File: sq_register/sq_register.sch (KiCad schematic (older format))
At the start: 1 part, among them P1 CONN_02X20

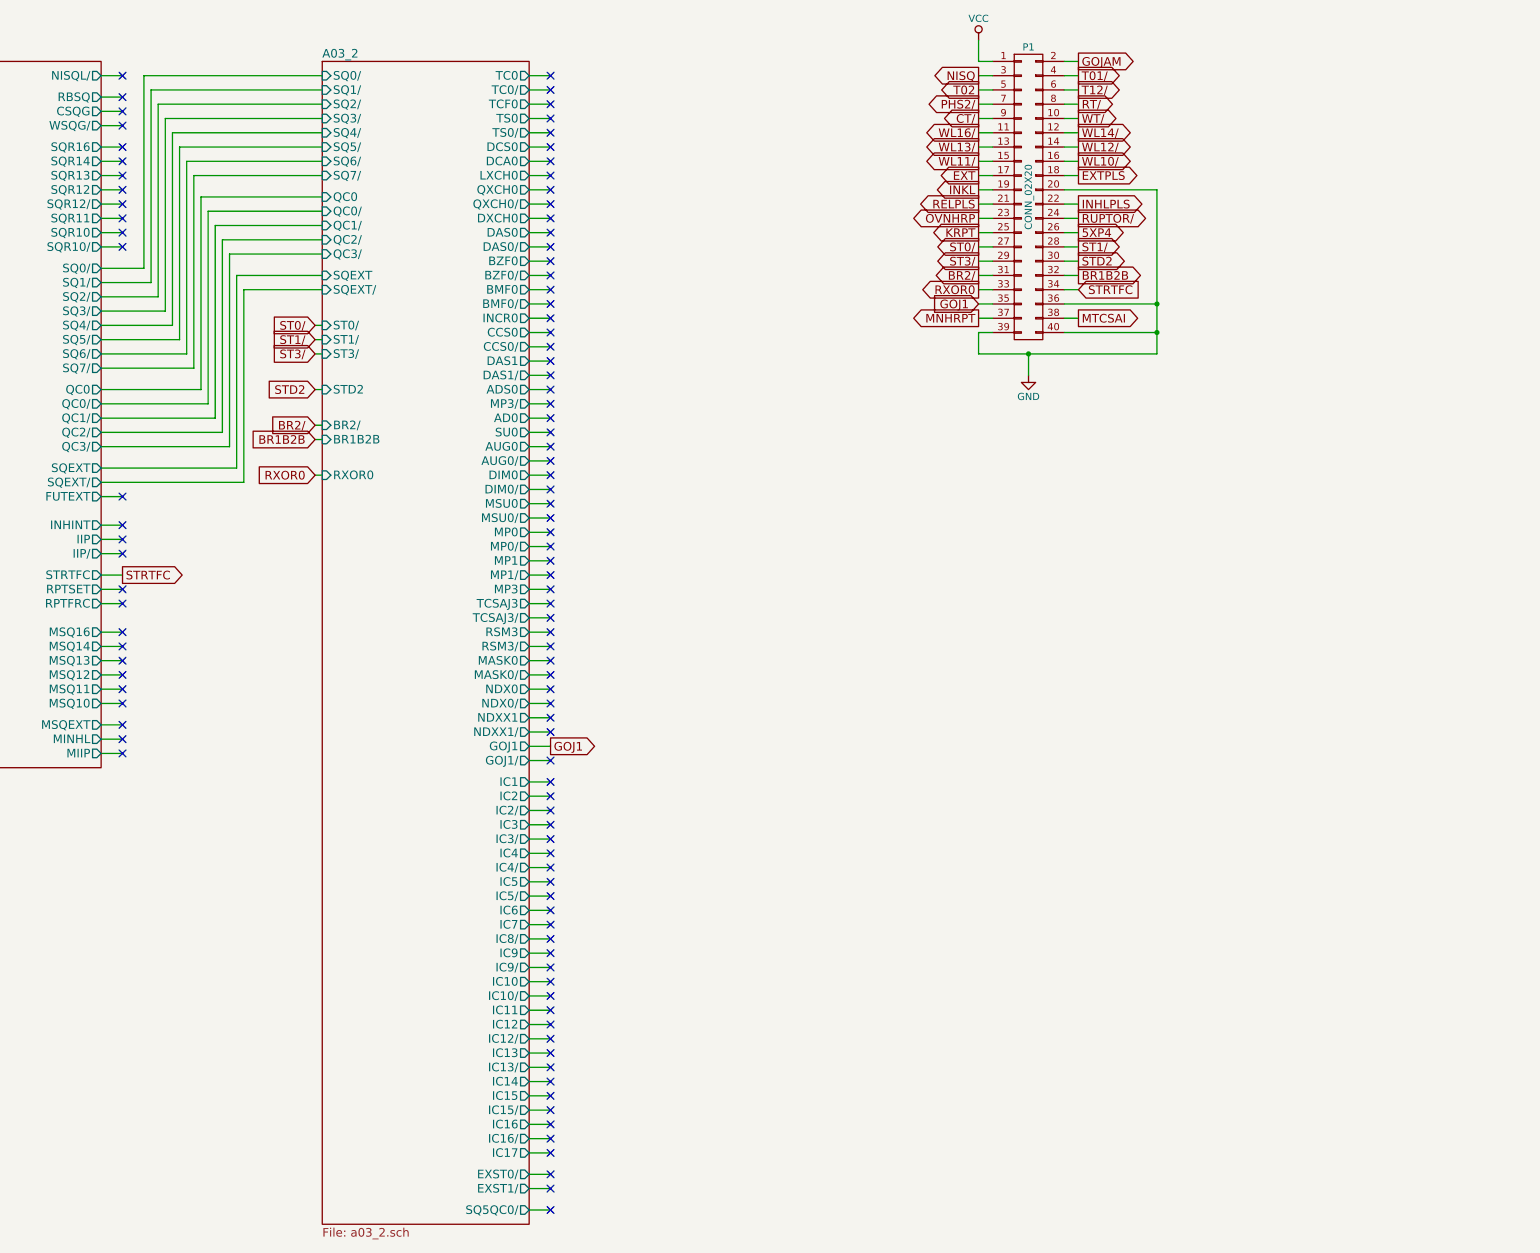
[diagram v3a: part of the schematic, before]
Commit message: Finished off the first page of the Stage Branch Decoding module.
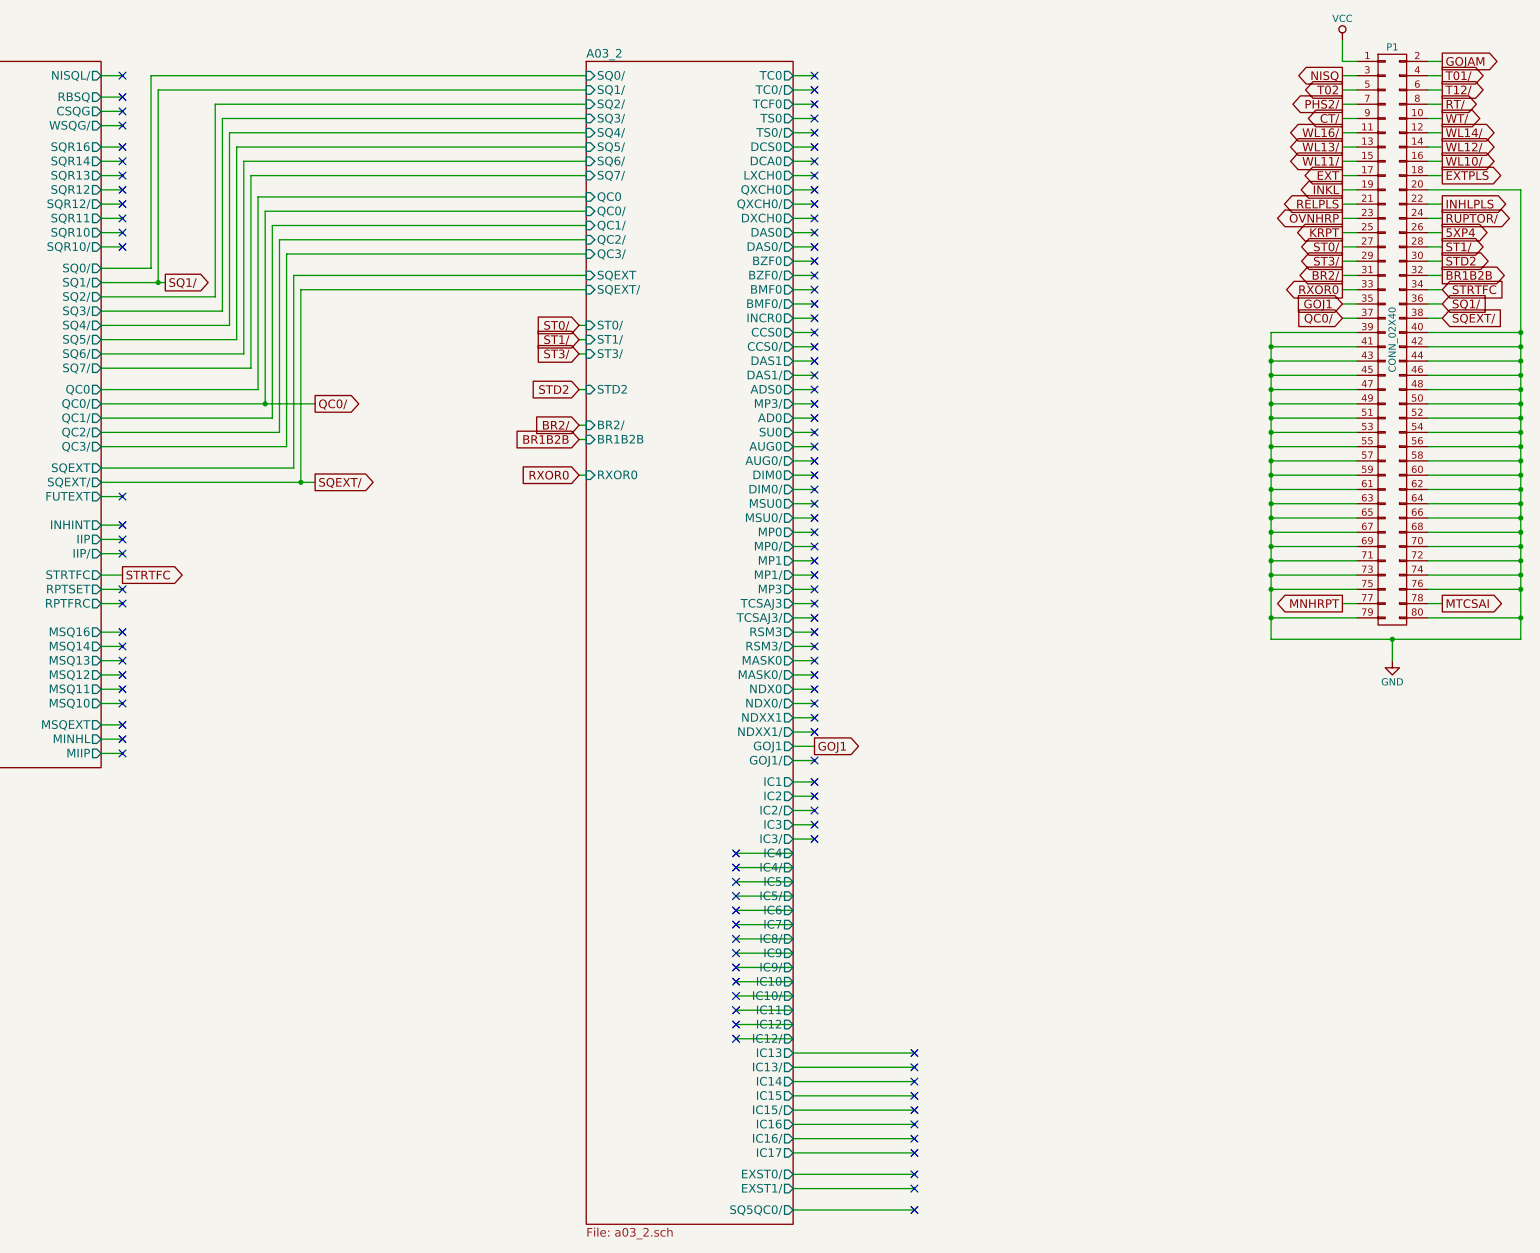
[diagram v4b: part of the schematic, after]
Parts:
- removed P1: CONN_02X20, symbol CONN_02X20
- added P1: CONN_02X40, symbol CONN_02X40
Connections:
- net 5XP4: now also P1.26 (P26)
- net BR1B2B: now also P1.32 (P32)
- net BR2/: now also P1.31 (P31)
- net CT/: now also P1.9 (P9)
- net EXT: now also P1.17 (P17)
- net EXTPLS: now also P1.18 (P18)
- net GND: now also P1.20 (P20), P1.39 (P39), P1.40 (P40), P1.41 (P41), P1.42 (P42), P1.43 (P43), P1.44 (P44), P1.45 (P45), P1.46 (P46), P1.47 (P47), P1.48 (P48), P1.49 (P49), P1.50 (P50), P1.51 (P51), P1.52 (P52), P1.53 (P53), P1.54 (P54), P1.55 (P55), P1.56 (P56), P1.57 (P57), P1.58 (P58), P1.59 (P59), P1.60 (P60), P1.61 (P61), P1.62 (P62), P1.63 (P63), P1.64 (P64), P1.65 (P65), P1.66 (P66), P1.67 (P67), P1.68 (P68), P1.69 (P69), P1.70 (P70), P1.71 (P71), P1.72 (P72), P1.73 (P73), P1.74 (P74), P1.75 (P75), P1.76 (P76), P1.79 (P79), P1.80 (P80)
- net GOJ1: now also P1.35 (P35)
- net GOJAM: now also P1.2 (P2)
- net INHLPLS: now also P1.22 (P22)
- net INKL: now also P1.19 (P19)
- net KRPT: now also P1.25 (P25)
- net MNHRPT: now also P1.77 (P77)
- net MTCSAI: now also P1.78 (P78)
- net NISQ: now also P1.3 (P3)
- net OVNHRP: now also P1.23 (P23)
- net PHS2/: now also P1.7 (P7)
- net RELPLS: now also P1.21 (P21)
- net RT/: now also P1.8 (P8)
- net RUPTOR/: now also P1.24 (P24)
- net RXOR0: now also P1.33 (P33)
- net ST0/: now also P1.27 (P27)
- net ST1/: now also P1.28 (P28)
- net ST3/: now also P1.29 (P29)
- net STD2: now also P1.30 (P30)
- net STRTFC: now also P1.34 (P34)
- net T01/: now also P1.4 (P4)
- net T02: now also P1.5 (P5)
- net T12/: now also P1.6 (P6)
- net VCC: now also P1.1 (P1)
- net WL10/: now also P1.16 (P16)
- net WL11/: now also P1.15 (P15)
- net WL12/: now also P1.14 (P14)
- net WL13/: now also P1.13 (P13)
- net WL14/: now also P1.12 (P12)
- net WL16/: now also P1.11 (P11)
- net WT/: now also P1.10 (P10)
- new net QC0/: P1.37 (P37)
- new net SQ1/: P1.36 (P36)
- new net SQEXT/: P1.38 (P38)

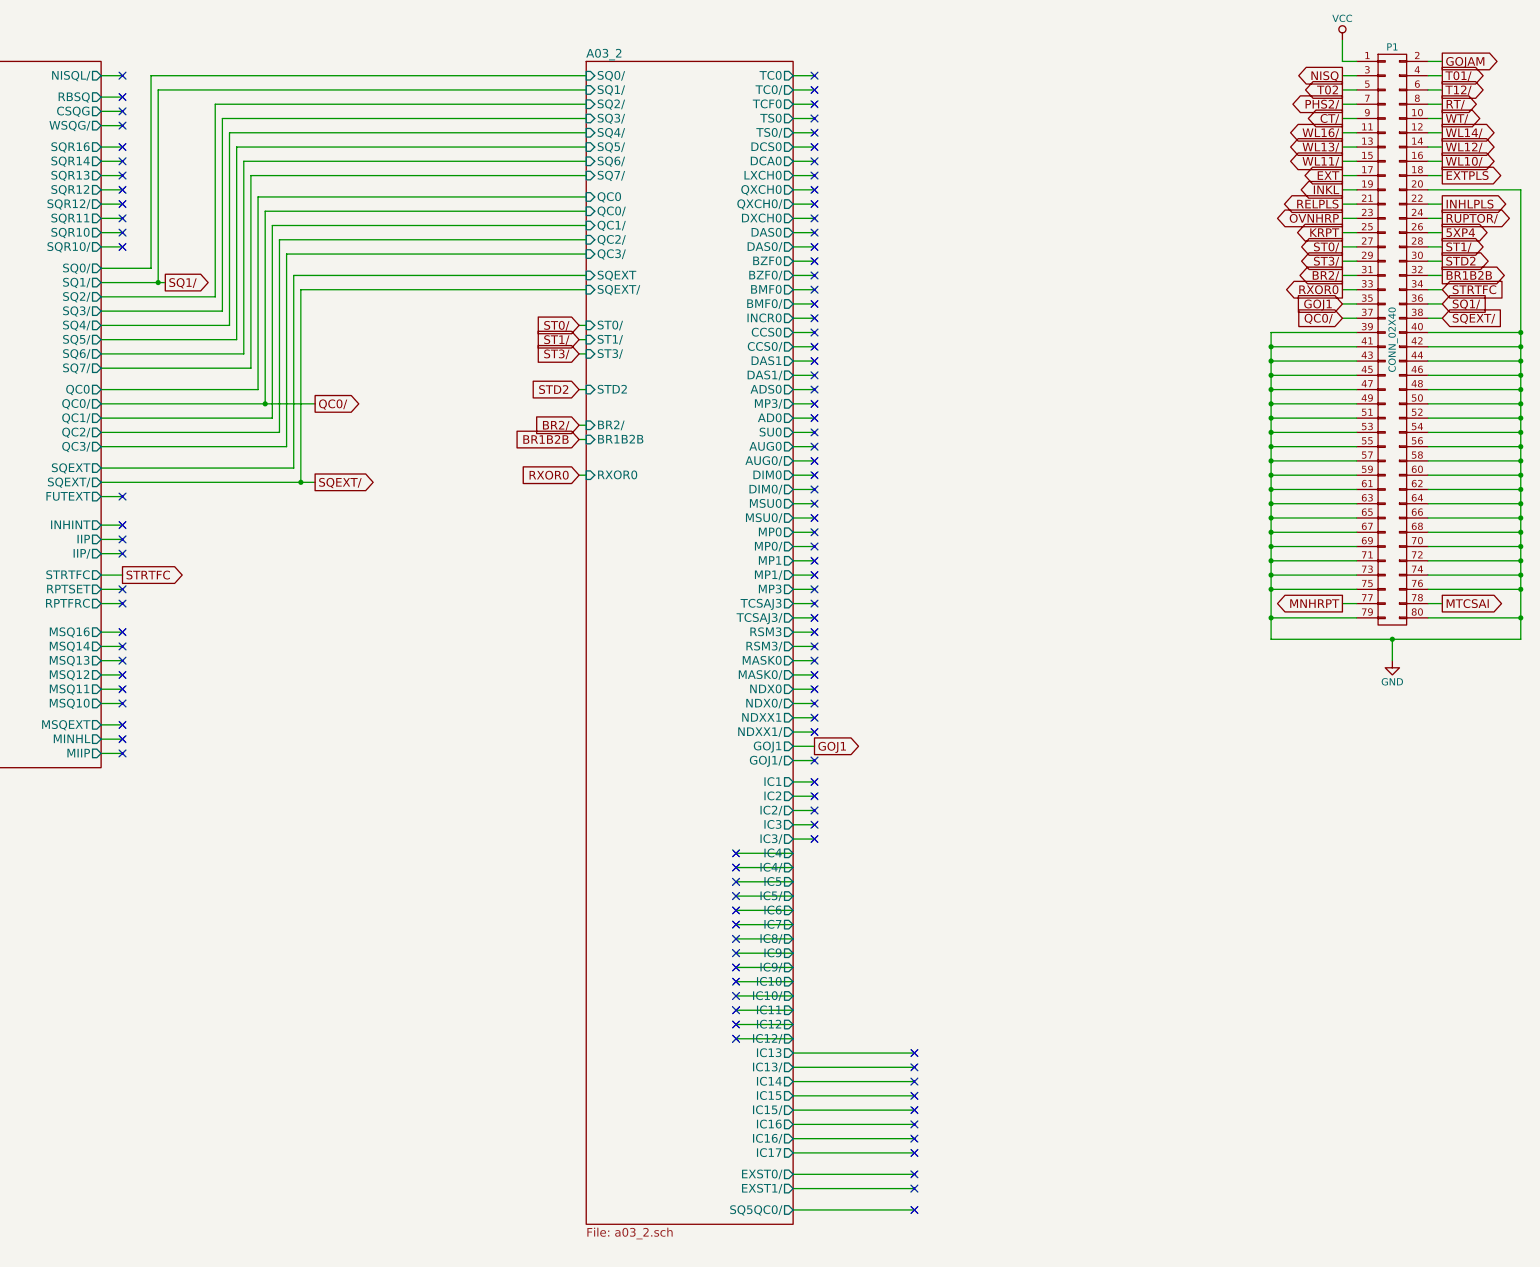
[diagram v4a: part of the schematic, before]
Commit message: Added page 2 of the Stage Branch Decoding module, and tied it into the rest of the system
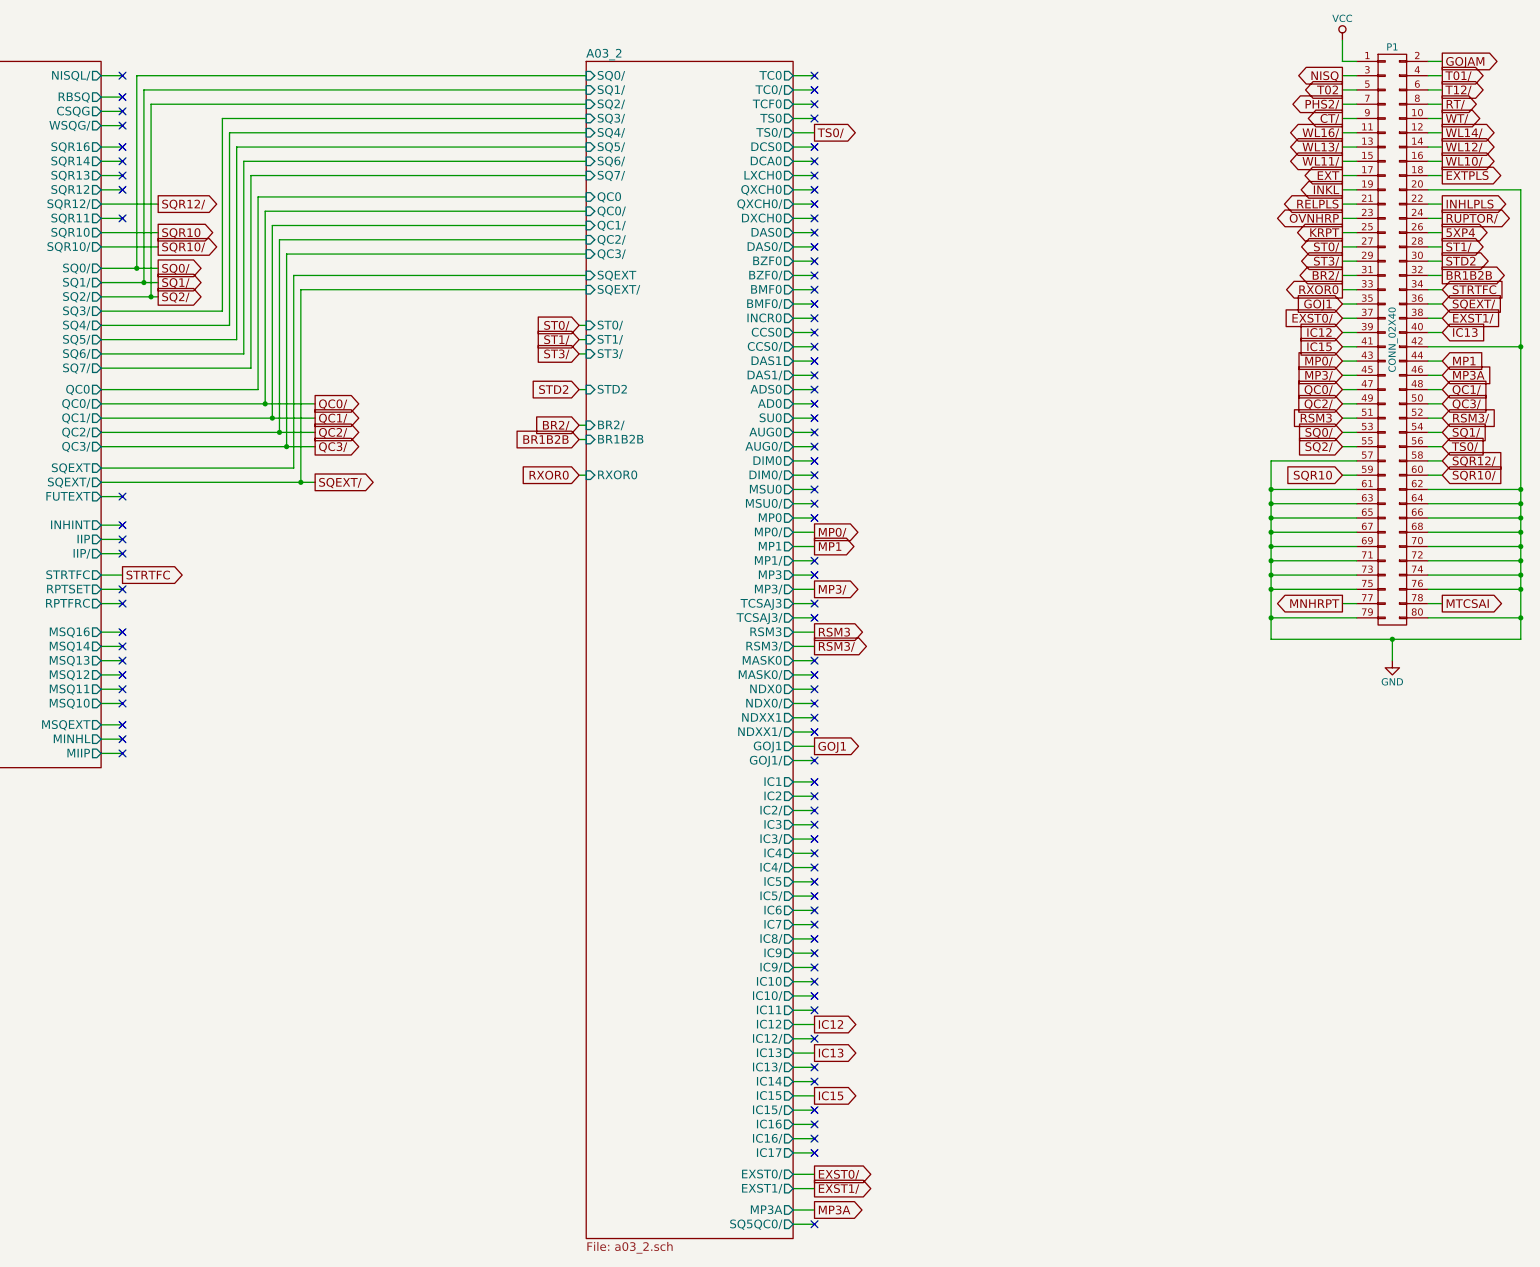
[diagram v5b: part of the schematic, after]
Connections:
- net GND: no longer P1.39 (P39), P1.40 (P40), P1.41 (P41), P1.43 (P43), P1.44 (P44), P1.45 (P45), P1.46 (P46), P1.47 (P47), P1.48 (P48), P1.49 (P49), P1.50 (P50), P1.51 (P51), P1.52 (P52), P1.53 (P53), P1.54 (P54), P1.55 (P55), P1.56 (P56), P1.58 (P58), P1.59 (P59), P1.60 (P60)
- net QC0/: now also P1.47 (P47); no longer P1.37 (P37)
- net SQ1/: now also P1.54 (P54); no longer P1.36 (P36)
- net SQEXT/: now also P1.36 (P36); no longer P1.38 (P38)
- new net EXST0/: P1.37 (P37)
- new net EXST1/: P1.38 (P38)
- new net IC12: P1.39 (P39)
- new net IC13: P1.40 (P40)
- new net IC15: P1.41 (P41)
- new net MP0/: P1.43 (P43)
- new net MP1: P1.44 (P44)
- new net MP3/: P1.45 (P45)
- new net MP3A: P1.46 (P46)
- new net QC1/: P1.48 (P48)
- new net QC2/: P1.49 (P49)
- new net QC3/: P1.50 (P50)
- new net RSM3: P1.51 (P51)
- new net RSM3/: P1.52 (P52)
- new net SQ0/: P1.53 (P53)
- new net SQ2/: P1.55 (P55)
- new net SQR10: P1.59 (P59)
- new net SQR10/: P1.60 (P60)
- new net SQR12/: P1.58 (P58)
- new net TS0/: P1.56 (P56)
- no-connect marks 105 -> 91

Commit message: Finished the second page of crosspoint generator 1 and tied it into the rest of the system.
Turns out most documentation online is wrong, and block 2 modules have 276 pins per module to the backplane, rather than the 140-144 that is quoted everywhere (those are block 1 figures). Instead of dealing with connector selection again, I opted to just add another row to the '128-pin' connector. I'll fix that more properly later
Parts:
- removed P1: CONN_02X40, symbol CONN_02X40
- added P1: DIN_41612_128P, symbol DIN_41612_128P
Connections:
- net 5XP4: now also P1.31 (31A)
- net BR1B2B: now also P1.26 (26A)
- net BR2/: now also P1.25 (25A)
- net CT/: now also P1.7 (7A)
- net EXST0/: now also P1.45 (13B)
- net EXST1/: now also P1.46 (14B)
- net EXT: now also P1.28 (28A)
- net EXTPLS: now also P1.29 (29A)
- net GND: now also P1.100 (4D), P1.101 (5D), P1.102 (6D), P1.103 (7D), P1.104 (8D), P1.105 (9D), P1.106 (10D), P1.107 (11D), P1.108 (12D), P1.109 (13D), P1.110 (14D), P1.111 (15D), P1.112 (16D), P1.113 (17D), P1.114 (18D), P1.115 (19D), P1.116 (20D), P1.117 (21D), P1.118 (22D), P1.119 (23D), P1.120 (24D), P1.121 (25D), P1.122 (26D), P1.123 (27D), P1.124 (28D), P1.125 (29D), P1.126 (30D), P1.127 (31D), P1.128 (32D), P1.130 (2E), P1.131 (3E), P1.132 (4E), P1.133 (5E), P1.134 (6E), P1.135 (7E), P1.136 (8E), P1.137 (9E), P1.138 (10E), P1.139 (11E), P1.140 (12E), P1.141 (13E), P1.142 (14E), P1.143 (15E), P1.144 (16E), P1.145 (17E), P1.146 (18E), P1.147 (19E), P1.148 (20E), P1.149 (21E), P1.150 (22E), P1.151 (23E), P1.152 (24E), P1.153 (25E), P1.154 (26E), P1.155 (27E), P1.156 (28E), P1.157 (29E), P1.158 (30E), P1.159 (31E), P1.160 (32E), P1.98 (2D), P1.99 (3D)
- net GOJ1: now also P1.56 (24B)
- net GOJAM: now also P1.1 (1A)
- net IC12: now also P1.90 (26C)
- net IC13: now also P1.92 (28C)
- net IC15: now also P1.94 (30C)
- net INKL: now also P1.15 (15A)
- net KRPT: now also P1.20 (20A)
- net MNHRPT: now also P1.33 (1B)
- net MP0/: now also P1.61 (29B)
- net MP1: now also P1.62 (30B)
- net MP3/: now also P1.64 (32B)
- net MP3A: now also P1.65 (1C)
- net MTCSAI: now also P1.32 (32A)
- net NISQ: now also P1.30 (30A)
- net OVNHRP: now also P1.18 (18A)
- net PHS2/: now also P1.5 (5A)
- net QC0/: now also P1.37 (5B)
- net QC1/: now also P1.38 (6B)
- net QC2/: now also P1.39 (7B)
- net QC3/: now also P1.40 (8B)
- net RELPLS: now also P1.17 (17A)
- net RSM3: now also P1.70 (6C)
- net RSM3/: now also P1.71 (7C)
- net RT/: now also P1.6 (6A)
- net RUPTOR/: now also P1.19 (19A)
- net RXOR0: now also P1.27 (27A)
- net SQ0/: now also P1.34 (2B)
- net SQ1/: now also P1.35 (3B)
- net SQ2/: now also P1.36 (4B)
- net SQEXT/: now also P1.44 (12B)
- net SQR10: now also P1.42 (10B)
- net SQR10/: now also P1.43 (11B)
- net SQR12/: now also P1.41 (9B)
- net ST0/: now also P1.21 (21A)
- net ST1/: now also P1.22 (22A)
- net ST3/: now also P1.24 (24A)
- net STD2: now also P1.23 (23A)
- net STRTFC: now also P1.47 (15B)
- net T01/: now also P1.2 (2A)
- net T02: now also P1.3 (3A)
- net T12/: now also P1.4 (4A)
- net TS0/: now also P1.77 (13C)
- net VCC: now also P1.129 (1E)
- net WL10/: now also P1.14 (14A)
- net WL11/: now also P1.13 (13A)
- net WL12/: now also P1.12 (12A)
- net WL13/: now also P1.11 (11A)
- net WL14/: now also P1.10 (10A)
- net WL16/: now also P1.9 (9A)
- net WT/: now also P1.8 (8A)
- new net ADS0: P1.48 (16B)
- new net CCS0: P1.49 (17B)
- new net CCS0/: P1.50 (18B)
- new net DAS0: P1.51 (19B)
- new net DAS0/: P1.52 (20B)
- new net DAS1: P1.53 (21B)
- new net DAS1/: P1.54 (22B)
- new net DXCH0: P1.55 (23B)
- new net GOJ1/: P1.57 (25B)
- new net IC1: P1.78 (14C)
- new net IC10: P1.87 (23C)
- new net IC10/: P1.88 (24C)
- new net IC11/: P1.89 (25C)
- new net IC12/: P1.91 (27C)
- new net IC14: P1.93 (29C)
- new net IC15/: P1.95 (31C)
- new net IC16: P1.96 (32C)
- new net IC16/: P1.97 (1D)
- new net IC2: P1.79 (15C)
- new net IC2/: P1.80 (16C)
- new net IC3: P1.81 (17C)
- new net IC4: P1.82 (18C)
- new net IC5: P1.83 (19C)
- new net IC5/: P1.84 (20C)
- new net IC8/: P1.85 (21C)
- new net IC9: P1.86 (22C)
- new net INHPLS: P1.16 (16A)
- new net MASK0: P1.58 (26B)
- new net MASK0/: P1.59 (27B)
- new net MP0: P1.60 (28B)
- new net MP3: P1.63 (31B)
- new net MSU0: P1.66 (2C)
- new net MSU0/: P1.67 (3C)
- new net NDX0/: P1.68 (4C)
- new net QXCH0/: P1.69 (5C)
- new net TC0: P1.72 (8C)
- new net TC0/: P1.73 (9C)
- new net TCF0: P1.74 (10C)
- new net TCSAJ3/: P1.75 (11C)
- new net TS0: P1.76 (12C)
- no-connect marks 91 -> 53
